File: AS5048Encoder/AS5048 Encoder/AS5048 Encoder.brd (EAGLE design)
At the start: 50 x 50 mm, 5 parts, among them X1 SI-50170

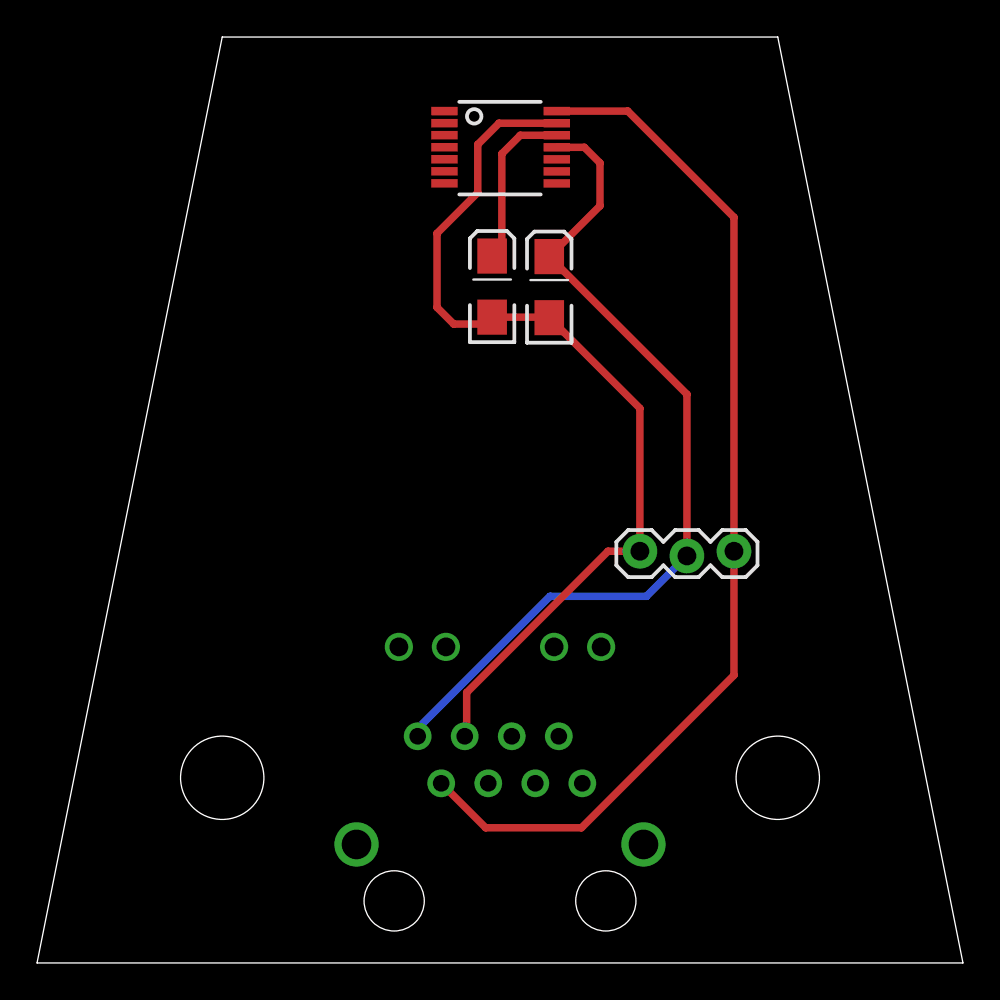
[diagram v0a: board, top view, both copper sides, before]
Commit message: rounded corners
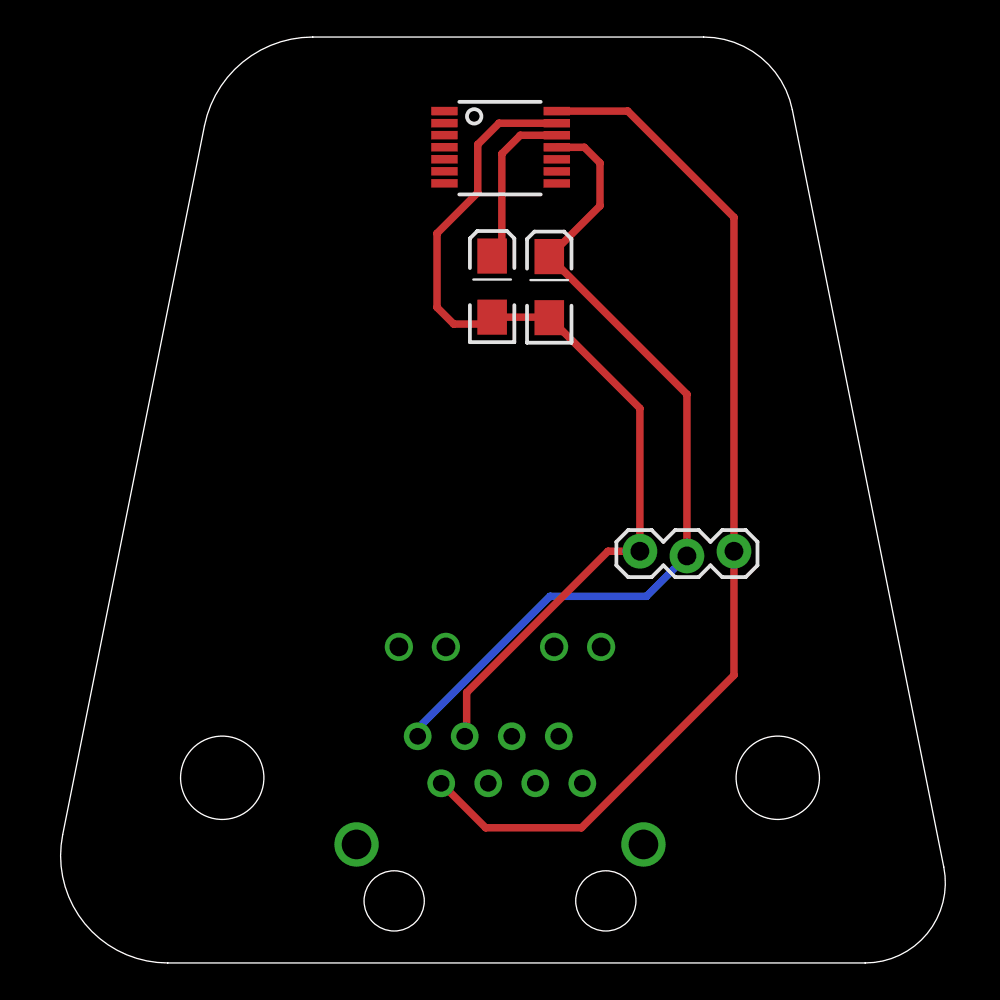
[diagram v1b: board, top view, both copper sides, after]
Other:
- board size 50 x 50 mm -> 47.8 x 50 mm
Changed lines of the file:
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@@
 <board>
 <plain>
-<wire x1="0" y1="0" x2="10" y2="50" width="0" layer="20"/>
-<wire x1="10" y1="50" x2="40" y2="50" width="0" layer="20"/>
-<wire x1="50" y1="0" x2="40" y2="50" width="0" layer="20"/>
+<wire x1="44.718565625" y1="0" x2="7.05936875" y2="0" width="0" layer="20"/>
+<wire x1="7.05936875" y1="0" x2="1.38445625" y2="6.92228125" width="0" layer="20" curve="-101.309951"/>
+<wire x1="1.38445625" y1="6.92228125" x2="9.0410375" y2="45.2051875" width="0" layer="20"/>
+<wire x1="9.0410375" y1="45.2051875" x2="14.889765625" y2="50" width="0" layer="20" curve="-78.690056"/>
+<wire x1="14.889765625" y1="50" x2="35.99700625" y2="50" width="0" layer="20"/>
+<wire x1="35.99700625" y1="50" x2="40.785053125" y2="46.074734375" width="0" layer="20" curve="-78.690139"/>
+<wire x1="40.785053125" y1="46.074734375" x2="48.964225" y2="5.178875" width="0" layer="20"/>
+<wire x1="48.964225" y1="5.178875" x2="44.718565625" y2="0" width="0" layer="20" curve="-101.309924"/>
 <rectangle x1="22.85508125" y1="33.382346875" x2="23.7796375" y2="33.400121875" layer="200" rot="R270"/>
 <rectangle x1="22.72173125" y1="33.373453125" x2="23.94855" y2="33.391234375" layer="200" rot="R270"/>
@@
 <hole x="10" y="10" drill="4.5"/>
 <hole x="40" y="10" drill="4.5"/>
-<wire x1="50" y1="0" x2="0" y2="0" width="0" layer="20"/>
 <dimension x1="10" y1="10" x2="40" y2="10" x3="25" y3="2.2" textsize="1.778" layer="22"/>
 <dimension x1="10" y1="10" x2="25" y2="44" x3="13.9954" y3="27" textsize="1.778" layer="22" dtype="vertical"/>

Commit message: moved encoder over
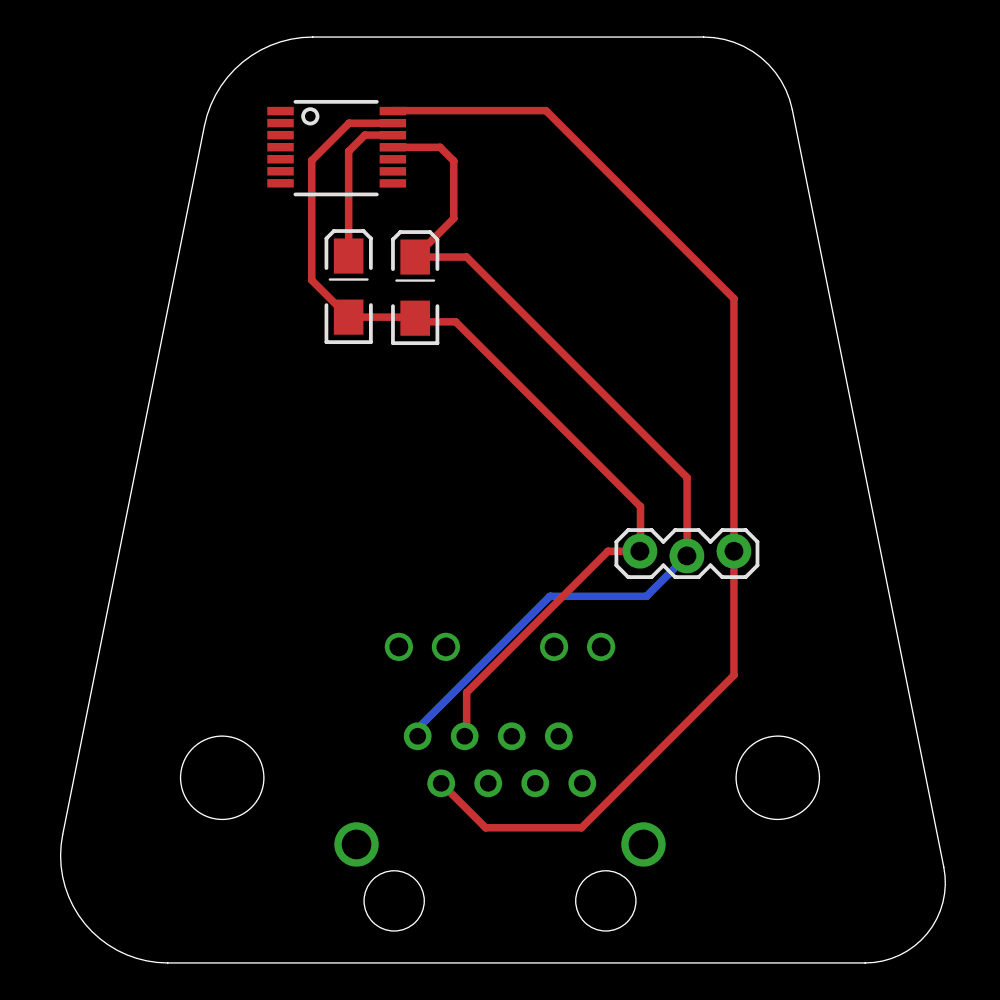
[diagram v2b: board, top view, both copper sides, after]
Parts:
- moved U$1 8.85 mm to (16.1, 44.0)
- moved C4 7.75 mm to (16.8, 36.5)
- moved C3 7.24 mm to (20.4, 36.5)
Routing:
- net PWM: track 56.9 -> 63.2 mm
- net VCC: track 46.9 -> 52.3 mm
- net GND: track 50.6 -> 51.9 mm
- net 3V3: track 9.12 -> 8.41 mm
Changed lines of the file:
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@@
 <setting verticaltext="up"/>
 </settings>
-<grid distance="1" unitdist="mil" unit="mm" style="lines" multiple="1" display="yes" altdistance="0.1" altunitdist="mm" altunit="mm"/>
+<grid distance="1" unitdist="mil" unit="mil" style="lines" multiple="1" display="yes" altdistance="0.1" altunitdist="mm" altunit="mm"/>
 <layers>
 <layer number="1" name="Top" color="4" fill="1" visible="yes" active="yes"/>
@@
 <hole x="40" y="10" drill="4.5"/>
 <dimension x1="10" y1="10" x2="40" y2="10" x3="25" y3="2.2" textsize="1.778" layer="22"/>
-<dimension x1="10" y1="10" x2="25" y2="44" x3="13.9954" y3="27" textsize="1.778" layer="22" dtype="vertical"/>
+<dimension x1="10" y1="10" x2="25" y2="44" x3="25.0444" y3="27" textsize="1.778" layer="22" dtype="vertical"/>
 </plain>
 <attributes>
@@
 </autorouter>
 <elements>
-<element name="C3" library="SparkFun-Passives" package="EIA3216-KIT" value="100nF" x="27.6598625" y="36.494021875" smashed="yes" rot="R90">
-<attribute name="VALUE" x="27.14818125" y="32.342659375" size="1.27" layer="27" rot="R270"/>
+<element name="C3" library="SparkFun-Passives" package="EIA3216-KIT" value="100nF" x="20.4208625" y="36.468621875" smashed="yes" rot="R90">
+<attribute name="VALUE" x="19.90918125" y="32.317259375" size="1.27" layer="27" rot="R270"/>
 </element>
-<element name="C4" library="SparkFun-Passives" package="EIA3216-KIT" value="10uF" x="24.57528125" y="36.52408125" smashed="yes" rot="R90">
-<attribute name="VALUE" x="24.231559375" y="32.662078125" size="1.27" layer="27" rot="R270"/>
+<element name="C4" library="SparkFun-Passives" package="EIA3216-KIT" value="10uF" x="16.82828125" y="36.52408125" smashed="yes" rot="R90">
+<attribute name="VALUE" x="16.484559375" y="32.662078125" size="1.27" layer="27" rot="R270"/>
 </element>
 <element name="JP1" library="SparkFun-Connectors" package="1X03_LOCK" value="" x="32.55431875" y="22.10614375" smashed="yes">
 <attribute name="VALUE" x="31.28431875" y="18.93114375" size="1.27" layer="27"/>
 </element>
-<element name="U$1" library="austriamicrosystems" package="TSOP14" value="AS5048" x="25" y="44" smashed="yes" rot="R270">
-<attribute name="VALUE" x="21.9283375" y="46.9731375" size="1.27" layer="27"/>
+<element name="U$1" library="austriamicrosystems" package="TSOP14" value="AS5048" x="16.15" y="44" smashed="yes" rot="R270">
+<attribute name="VALUE" x="13.0783375" y="46.9731375" size="1.27" layer="27"/>
 </element>
 <element name="X1" library="con-stewart" package="SI-50170" value="SI-50170" x="25" y="6.4" rot="MR0">
@@
 <contactref element="U$1" pad="13"/>
 <contactref element="X1" pad="3"/>
-<wire x1="28.06541875" y1="45.34568125" x2="24.94568125" y2="45.34568125" width="0.4064" layer="1"/>
-<wire x1="24.94568125" y1="45.34568125" x2="23.8" y2="44.2" width="0.4064" layer="1"/>
-<wire x1="23.8" y1="44.2" x2="23.8" y2="41.6" width="0.4064" layer="1"/>
-<wire x1="23.8" y1="41.6" x2="21.6" y2="39.4" width="0.4064" layer="1"/>
-<wire x1="21.6" y1="39.4" x2="21.6" y2="35.4" width="0.4064" layer="1"/>
-<wire x1="21.6" y1="35.4" x2="22.5" y2="34.5" width="0.4064" layer="1"/>
-<wire x1="22.5" y1="34.5" x2="24.2012" y2="34.5" width="0.4064" layer="1"/>
-<wire x1="24.2012" y1="34.5" x2="24.57528125" y2="34.87408125" width="0.4064" layer="1"/>
-<wire x1="24.57528125" y1="34.87408125" x2="27.629803125" y2="34.87408125" width="0.4064" layer="1"/>
-<wire x1="27.629803125" y1="34.87408125" x2="27.6598625" y2="34.844021875" width="0.4064" layer="1"/>
-<wire x1="32.55431875" y1="22.23314375" x2="32.55431875" y2="29.949565625" width="0.4064" layer="1"/>
-<wire x1="32.55431875" y1="29.949565625" x2="27.6598625" y2="34.844021875" width="0.4064" layer="1"/>
 <wire x1="32.55431875" y1="22.23314375" x2="30.83314375" y2="22.23314375" width="0.4064" layer="1"/>
 <wire x1="30.83314375" y1="22.23314375" x2="23.2" y2="14.6" width="0.4064" layer="1"/>
 <wire x1="23.2" y1="14.6" x2="23.2" y2="12.347" width="0.4064" layer="1"/>
 <wire x1="23.2" y1="12.347" x2="23.095" y2="12.242" width="0.4064" layer="1"/>
+<wire x1="19.21541875" y1="45.34568125" x2="16.84688125" y2="45.34568125" width="0.4064" layer="1"/>
+<wire x1="16.84688125" y1="45.34568125" x2="14.8336" y2="43.3324" width="0.4064" layer="1"/>
+<wire x1="14.8336" y1="43.3324" x2="14.8336" y2="36.8687625" width="0.4064" layer="1"/>
+<wire x1="14.8336" y1="36.8687625" x2="16.82828125" y2="34.87408125" width="0.4064" layer="1"/>
+<wire x1="16.82828125" y1="34.87408125" x2="20.365403125" y2="34.87408125" width="0.4064" layer="1"/>
+<wire x1="20.365403125" y1="34.87408125" x2="20.4208625" y2="34.818621875" width="0.4064" layer="1"/>
+<wire x1="20.4208625" y1="34.818621875" x2="20.4208625" y2="34.7733375" width="0.4064" layer="1"/>
+<wire x1="20.4208625" y1="34.7733375" x2="20.574" y2="34.6202" width="0.4064" layer="1"/>
+<wire x1="20.574" y1="34.6202" x2="22.606" y2="34.6202" width="0.4064" layer="1"/>
+<wire x1="22.606" y1="34.6202" x2="32.5882" y2="24.638" width="0.4064" layer="1"/>
+<wire x1="32.5882" y1="24.638" x2="32.5882" y2="22.267025" width="0.4064" layer="1"/>
+<wire x1="32.5882" y1="22.267025" x2="32.55431875" y2="22.23314375" width="0.4064" layer="1"/>
 </signal>
 <signal name="VCC">
@@
 <contactref element="U$1" pad="11"/>
 <contactref element="X1" pad="1"/>
-<wire x1="27.6598625" y1="38.144021875" x2="30.4" y2="40.884159375" width="0.4064" layer="1"/>
-<wire x1="30.4" y1="40.884159375" x2="30.4" y2="43.2" width="0.4064" layer="1"/>
-<wire x1="30.4" y1="43.2" x2="29.55431875" y2="44.04568125" width="0.4064" layer="1"/>
-<wire x1="29.55431875" y1="44.04568125" x2="28.06541875" y2="44.04568125" width="0.4064" layer="1"/>
-<wire x1="35.09431875" y1="21.97914375" x2="35.09431875" y2="30.709565625" width="0.4064" layer="1"/>
-<wire x1="35.09431875" y1="30.709565625" x2="27.6598625" y2="38.144021875" width="0.4064" layer="1"/>
 <wire x1="20.555" y1="12.242" x2="20.555" y2="12.655" width="0.4064" layer="16"/>
 <wire x1="20.555" y1="12.655" x2="27.7" y2="19.8" width="0.4064" layer="16"/>
 <wire x1="27.7" y1="19.8" x2="32.915175" y2="19.8" width="0.4064" layer="16"/>
 <wire x1="32.915175" y1="19.8" x2="35.09431875" y2="21.97914375" width="0.4064" layer="16"/>
+<wire x1="19.21541875" y1="44.04568125" x2="21.76571875" y2="44.04568125" width="0.4064" layer="1"/>
+<wire x1="21.76571875" y1="44.04568125" x2="22.5044" y2="43.307" width="0.4064" layer="1"/>
+<wire x1="22.5044" y1="43.307" x2="22.5044" y2="40.202159375" width="0.4064" layer="1"/>
+<wire x1="22.5044" y1="40.202159375" x2="20.4208625" y2="38.118621875" width="0.4064" layer="1"/>
+<wire x1="20.4208625" y1="38.118621875" x2="23.196978125" y2="38.118621875" width="0.4064" layer="1"/>
+<wire x1="23.196978125" y1="38.118621875" x2="35.1028" y2="26.2128" width="0.4064" layer="1"/>
+<wire x1="35.1028" y1="26.2128" x2="35.1028" y2="21.987625" width="0.4064" layer="1"/>
+<wire x1="35.1028" y1="21.987625" x2="35.09431875" y2="21.97914375" width="0.4064" layer="1"/>
 </signal>
 <signal name="3V3">
 <contactref element="C4" pad="A"/>
 <contactref element="U$1" pad="12"/>
-<wire x1="24.57528125" y1="38.17408125" x2="25.1" y2="38.6988" width="0.4064" layer="1"/>
-<wire x1="25.1" y1="38.6988" x2="25.1" y2="43.7" width="0.4064" layer="1"/>
-<wire x1="25.1" y1="43.7" x2="26.09568125" y2="44.69568125" width="0.4064" layer="1"/>
-<wire x1="26.09568125" y1="44.69568125" x2="28.06541875" y2="44.69568125" width="0.4064" layer="1"/>
+<wire x1="16.82828125" y1="38.17408125" x2="16.82828125" y2="43.82848125" width="0.4064" layer="1"/>
+<wire x1="16.82828125" y1="43.82848125" x2="17.7038" y2="44.704" width="0.4064" layer="1"/>
+<wire x1="17.7038" y1="44.704" x2="19.2071" y2="44.704" width="0.4064" layer="1"/>
+<wire x1="19.2071" y1="44.704" x2="19.21541875" y2="44.69568125" width="0.4064" layer="1"/>
 </signal>
 <signal name="PWM">
@@
 <contactref element="JP1" pad="3"/>
 <contactref element="X1" pad="2"/>
-<wire x1="37.63431875" y1="22.23314375" x2="37.63431875" y2="40.26568125" width="0.4064" layer="1"/>
-<wire x1="37.63431875" y1="40.26568125" x2="31.9" y2="46" width="0.4064" layer="1"/>
-<wire x1="31.9" y1="46" x2="28.06541875" y2="46" width="0.4064" layer="1"/>
 <wire x1="21.825" y1="9.702" x2="24.227" y2="7.3" width="0.4064" layer="1"/>
 <wire x1="24.227" y1="7.3" x2="29.4" y2="7.3" width="0.4064" layer="1"/>
 <wire x1="29.4" y1="7.3" x2="37.63431875" y2="15.53431875" width="0.4064" layer="1"/>
 <wire x1="37.63431875" y1="15.53431875" x2="37.63431875" y2="22.23314375" width="0.4064" layer="1"/>
+<wire x1="37.63431875" y1="22.23314375" x2="37.63431875" y2="35.87328125" width="0.4064" layer="1"/>
+<wire x1="37.63431875" y1="35.87328125" x2="27.4828" y2="46.0248" width="0.4064" layer="1"/>
+<wire x1="27.4828" y1="46.0248" x2="19.24021875" y2="46.0248" width="0.4064" layer="1"/>
+<wire x1="19.24021875" y1="46.0248" x2="19.21541875" y2="46" width="0.4064" layer="1"/>
 </signal>
 </signals>
